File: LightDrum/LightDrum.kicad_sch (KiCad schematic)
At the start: 5 parts, among them U101 STR485

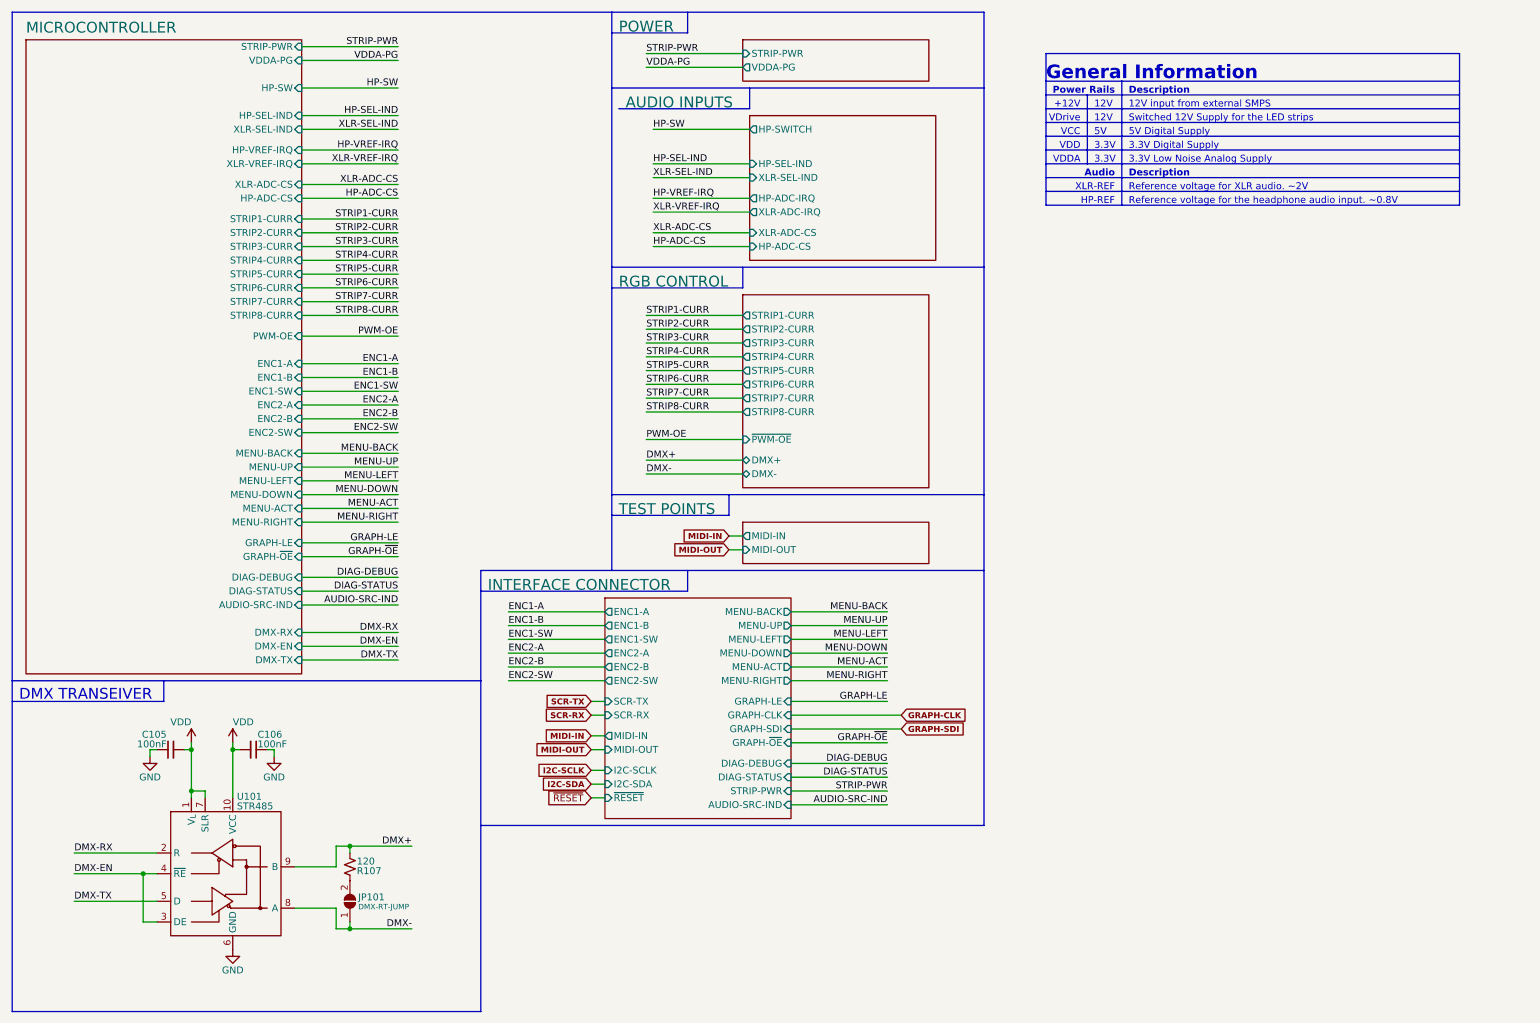
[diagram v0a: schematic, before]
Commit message: Replace relays and SWD conn
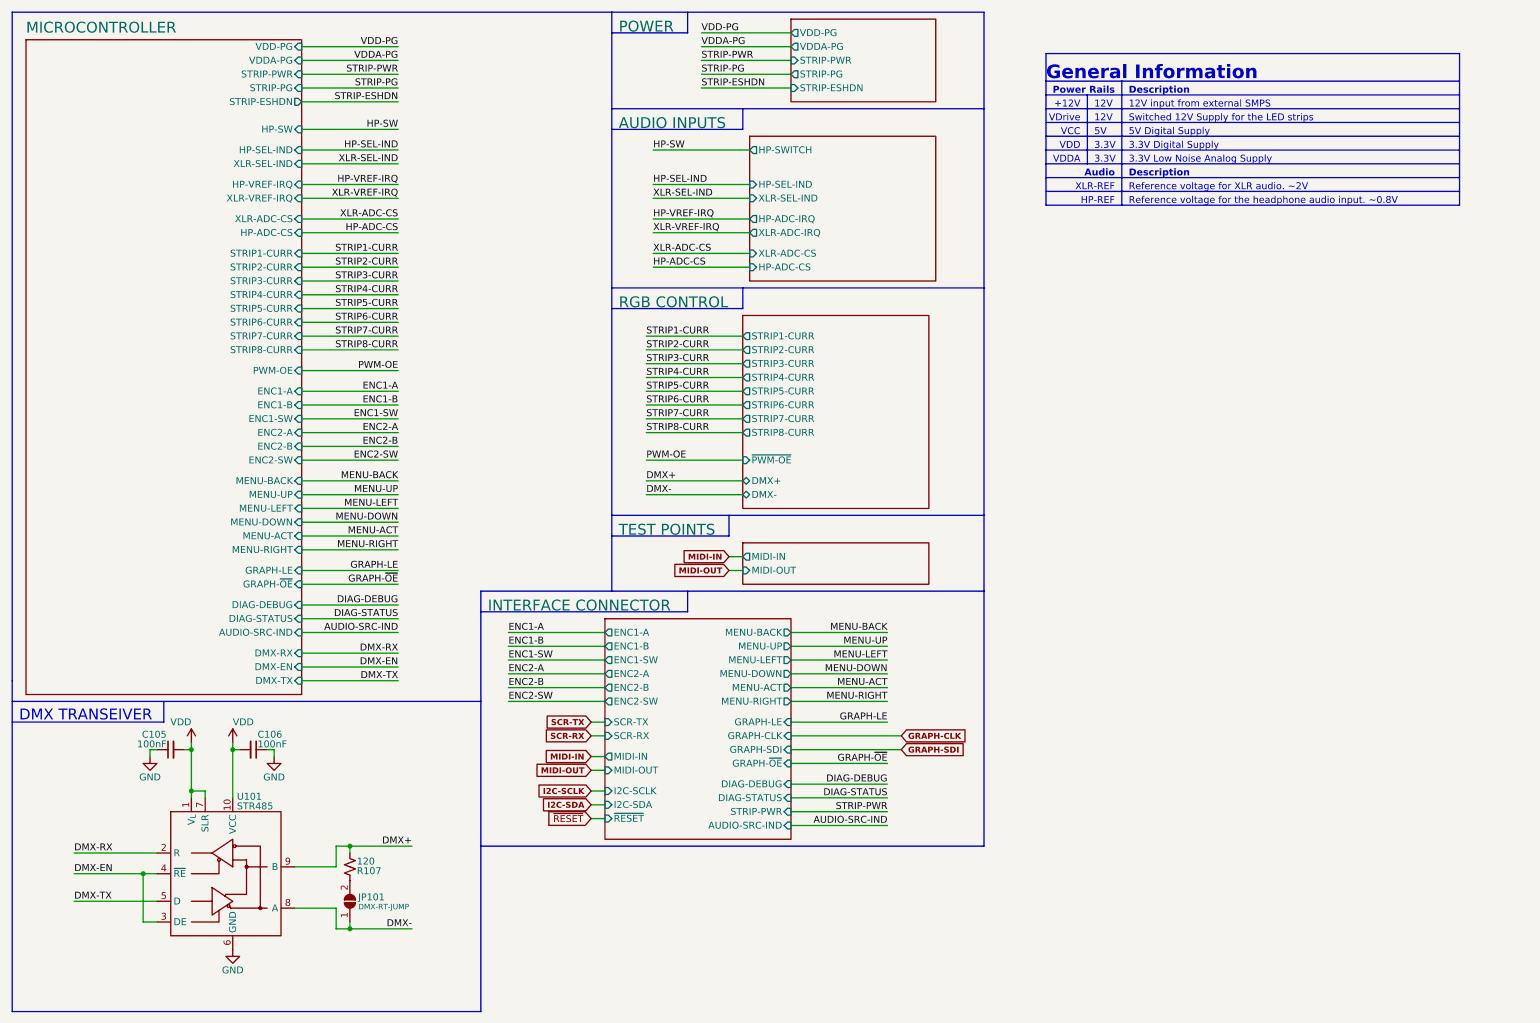
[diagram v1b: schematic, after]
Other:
- sheet MICROCONTROLLER ports: added STRIP-ESHDN, STRIP-PG, VDD-PG; removed none
- sheet POWER ports: added STRIP-ESHDN, STRIP-PG, VDD-PG; removed none

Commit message: Preliminary schematic lock - Starting PCB layout
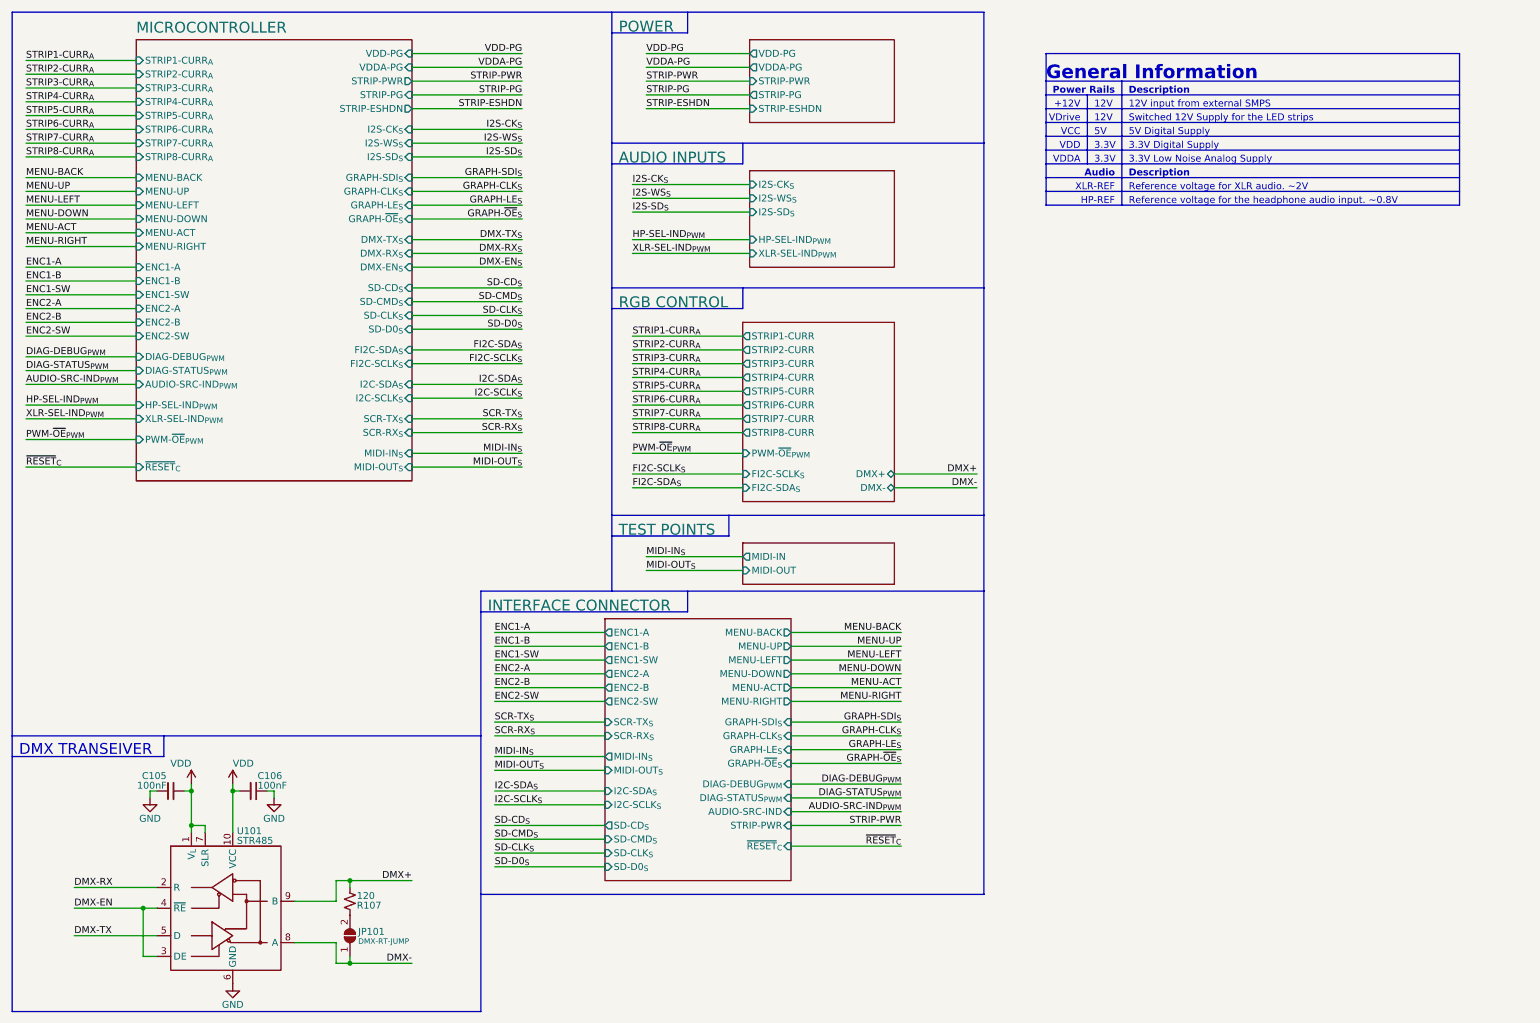
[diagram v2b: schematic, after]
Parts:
- C105, C106: SupplierPN (none) -> 1276-1043-1-ND
- R107: footprint Resistor_SMD:R_0603_1608Metric -> Resistor_SMD:R_0402_1005Metric; SupplierPN (none) -> 311-120LRCT-ND
- U101: SupplierPN (none) -> 497-18335-1-ND
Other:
- sheet AUDIO INPUTS ports: added HP-SEL-IND_{PWM}, I2S-CK_{S}, I2S-SD_{S}, I2S-WS_{S}, XLR-SEL-IND_{PWM}; removed HP-ADC-CS, HP-ADC-IRQ, HP-SEL-IND, HP-SWITCH, XLR-ADC-CS, XLR-ADC-IRQ, XLR-SEL-IND
- sheet INTERFACE CONNECTOR ports: added DIAG-DEBUG_{PWM}, DIAG-STATUS_{PWM}, GRAPH-CLK_{S}, GRAPH-LE_{S}, GRAPH-SDI_{S}, GRAPH-~{OE}_{S}, I2C-SCLK_{S}, I2C-SDA_{S}, MIDI-IN_{S}, MIDI-OUT_{S}, SCR-RX_{S}, SCR-TX_{S}, SD-CD_{S}, SD-CLK_{S}, SD-CMD_{S}, SD-D0_{S}, ~{RESET}_{C}; removed DIAG-DEBUG, DIAG-STATUS, GRAPH-CLK, GRAPH-LE, GRAPH-SDI, GRAPH-~{OE}, I2C-SCLK, I2C-SDA, MIDI-IN, MIDI-OUT, SCR-RX, SCR-TX, ~{RESET}
- sheet MICROCONTROLLER ports: added AUDIO-SRC-IND_{PWM}, DIAG-DEBUG_{PWM}, DIAG-STATUS_{PWM}, DMX-EN_{S}, DMX-RX_{S}, DMX-TX_{S}, FI2C-SCLK_{S}, FI2C-SDA_{S}, GRAPH-CLK_{S}, GRAPH-LE_{S}, GRAPH-SDI_{S}, GRAPH-~{OE}_{S}, HP-SEL-IND_{PWM}, I2C-SCLK_{S}, I2C-SDA_{S}, I2S-CK_{S}, I2S-SD_{S}, I2S-WS_{S}, MIDI-IN_{S}, MIDI-OUT_{S}, PWM-~{OE}_{PWM}, SCR-RX_{S}, SCR-TX_{S}, SD-CD_{S}, SD-CLK_{S}, SD-CMD_{S}, SD-D0_{S}, STRIP1-CURR_{A}, STRIP2-CURR_{A}, STRIP3-CURR_{A}, STRIP4-CURR_{A}, STRIP5-CURR_{A}, STRIP6-CURR_{A}, STRIP7-CURR_{A}, STRIP8-CURR_{A}, XLR-SEL-IND_{PWM}, ~{RESET}_{C}; removed AUDIO-SRC-IND, DIAG-DEBUG, DIAG-STATUS, DMX-EN, DMX-RX, DMX-TX, GRAPH-LE, GRAPH-~{OE}, HP-ADC-CS, HP-SEL-IND, HP-SW, HP-VREF-IRQ, PWM-OE, STRIP1-CURR, STRIP2-CURR, STRIP3-CURR, STRIP4-CURR, STRIP5-CURR, STRIP6-CURR, STRIP7-CURR, STRIP8-CURR, XLR-ADC-CS, XLR-SEL-IND, XLR-VREF-IRQ
- sheet RGB CONTROL ports: added FI2C-SCLK_{S}, FI2C-SDA_{S}, PWM-~{OE}_{PWM}; removed ~{PWM-OE}
- moved on the sheet: C105, C106, JP101, R107, U101

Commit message: Component placement complete
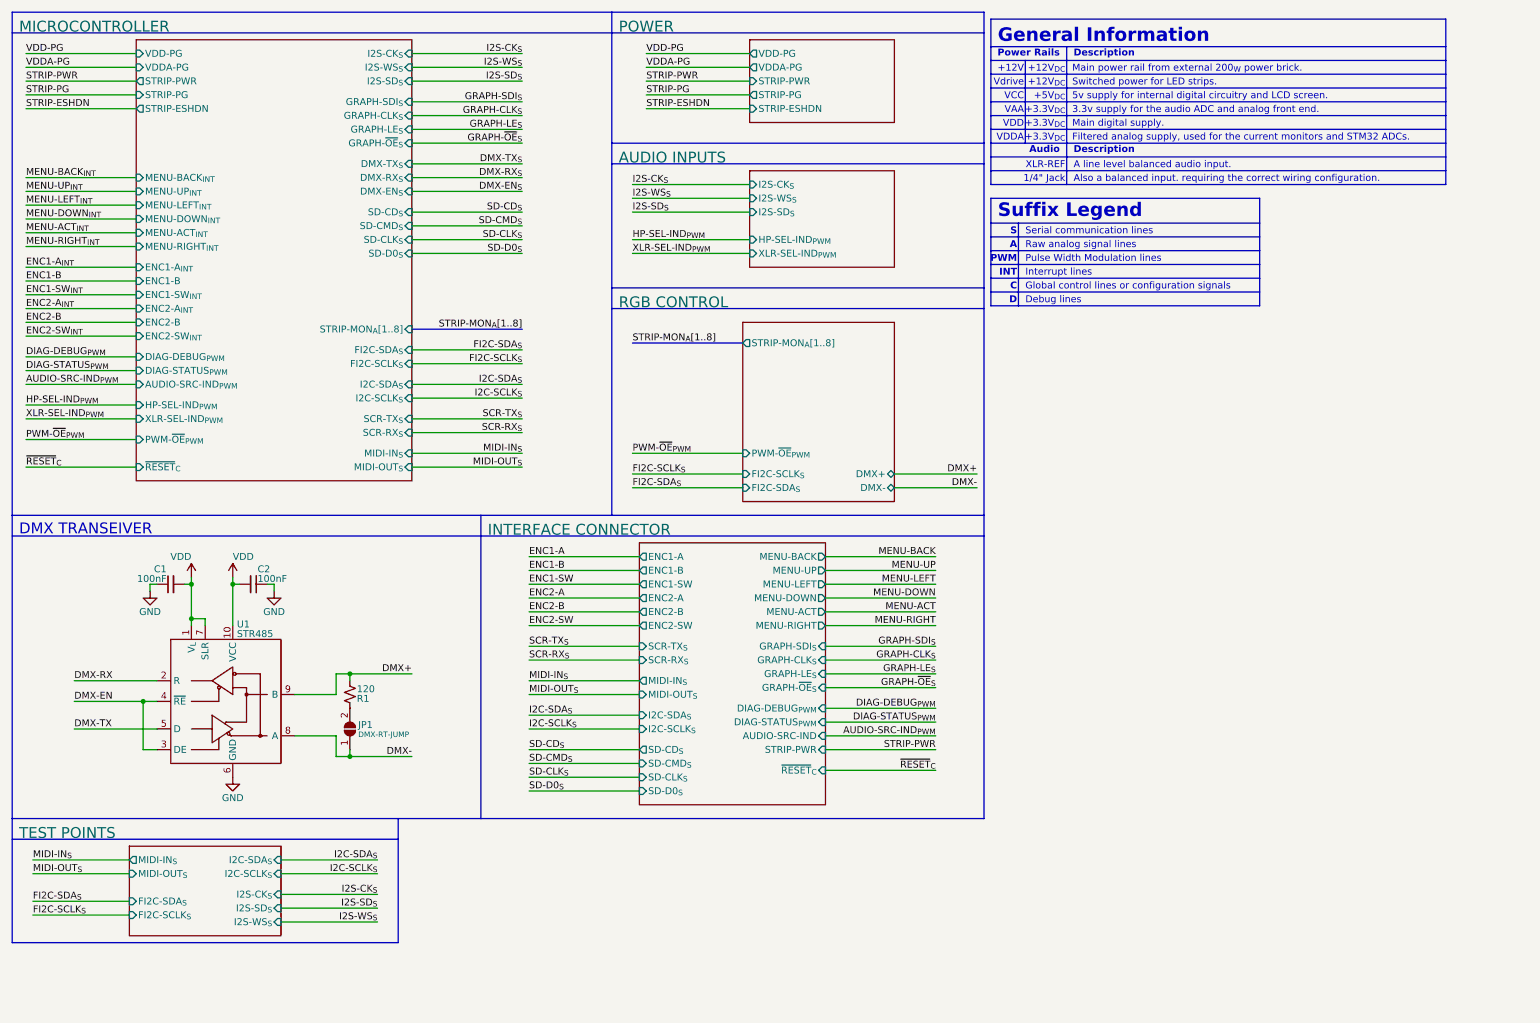
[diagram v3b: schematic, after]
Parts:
- renumbered C105 to C1, C106 to C2, JP101 to JP1, R107 to R1, U101 to U1
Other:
- sheet MICROCONTROLLER ports: added ENC1-A_{INT}, ENC1-SW_{INT}, ENC2-A_{INT}, ENC2-SW_{INT}, MENU-ACT_{INT}, MENU-BACK_{INT}, MENU-DOWN_{INT}, MENU-LEFT_{INT}, MENU-RIGHT_{INT}, MENU-UP_{INT}, STRIP-MON_{A}[1..8]; removed ENC1-A, ENC1-SW, ENC2-A, ENC2-SW, MENU-ACT, MENU-BACK, MENU-DOWN, MENU-LEFT, MENU-RIGHT, MENU-UP, STRIP1-CURR_{A}, STRIP2-CURR_{A}, STRIP3-CURR_{A}, STRIP4-CURR_{A}, STRIP5-CURR_{A}, STRIP6-CURR_{A}, STRIP7-CURR_{A}, STRIP8-CURR_{A}
- sheet RGB CONTROL ports: added STRIP-MON_{A}[1..8]; removed STRIP1-CURR, STRIP2-CURR, STRIP3-CURR, STRIP4-CURR, STRIP5-CURR, STRIP6-CURR, STRIP7-CURR, STRIP8-CURR
- sheet TEST POINTS ports: added FI2C-SCLK_{S}, FI2C-SDA_{S}, I2C-SCLK_{S}, I2C-SDA_{S}, I2S-CK_{S}, I2S-SD_{S}, I2S-WS_{S}, MIDI-IN_{S}, MIDI-OUT_{S}; removed MIDI-IN, MIDI-OUT
- note added: "+12V_{DC}"
- note added: "+3.3V_{DC}"
- note added: "+5V_{DC}"
- note added: "1/4" Jack"
- note added: "3.3v supply for the audio ADC and analog front end."
- note added: "5v supply for internal digital circuitry and LCD screen."
- note added: "A"
- note added: "A line level balanced audio input."
- note added: "Also a balanced input. requiring the correct wiring configuration."
- note added: "C"
- note added: "D"
- note added: "Debug lines"
- note added: "Filtered analog supply, used for the current monitors and STM32 ADCs."
- note added: "Global control lines or configuration signals"
- note added: "INT"
- note added: "Interrupt lines"
- note added: "Main digital supply."
- note added: "Main power rail from external 200_{W} power brick."
- note added: "PWM"
- note added: "Pulse Width Modulation lines"
- note added: "Raw analog signal lines"
- note added: "S"
- note added: "Serial communication lines"
- note added: "Suffix Legend"
- note added: "Switched power for LED strips."
- note added: "VAA"
- note added: "Vdrive"
- note removed: "12V"
- note removed: "12V input from external SMPS"
- note removed: "3.3V"
- note removed: "3.3V Digital Supply"
- note removed: "3.3V Low Noise Analog Supply"
- note removed: "5V"
- note removed: "5V Digital Supply"
- note removed: "HP-REF"
- note removed: "Reference voltage for XLR audio. ~2V"
- note removed: "Reference voltage for the headphone audio input. ~0.8V"
- note removed: "Switched 12V Supply for the LED strips"
- note removed: "VDrive"
- moved on the sheet: C1, C2, JP1, R1, U1
